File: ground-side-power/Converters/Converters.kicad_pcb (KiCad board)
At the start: 2 copper layers, 82.8 x 74.4 mm, 43 parts, among them J10 Conn_01x03_Female, J11 Ground Connections, J12 Conn_01x04_Female, J13 DAQ Voltage Sensing, J14 DAQ Current Sensing, J27 Conn_01x02_Female, U1 TPS55340, U2 K7805-3AR3, U4 INA180, U5 INA180

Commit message: implemented comments
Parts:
- added ?: , , F.Cu at (108.5, 71.1)
- added ?: , , F.Cu at (181.1, 135.6)
- added ?: , , F.Cu at (181.1, 71.1)
- added ?: , , F.Cu at (108.5, 135.6)
- added G***: LOGO, rlcs:rocketry_logo_small, F.Cu at (176.8, 125.5)
- added TP1: TestPoint, TestPoint:TestPoint_Plated_Hole_D2.0mm, F.Cu at (166.6, 111.0)
- added TP2: TestPoint, TestPoint:TestPoint_Plated_Hole_D2.0mm, F.Cu at (180.8, 88.4)
- added TP3: TestPoint, TestPoint:TestPoint_Plated_Hole_D2.0mm, F.Cu at (133.9, 76.7)
- F2: renamed from F3; value 0685T4000-01 -> 4A 0685T4000-01
- moved C10 51.8 mm to (137.7, 83.1), turned to 180 degrees
- moved C7 48.4 mm to (125.2, 81.0), turned to 180 degrees
- moved C9 41.9 mm to (144.0, 83.1), turned to 180 degrees
- moved C8 31.8 mm to (150.1, 83.1), turned to 180 degrees
- moved L1 19.8 mm to (173.7, 85.9), turned to 180 degrees
- moved C6 2.54 mm to (137.2, 99.1)
- moved R11 0.52 mm to (118.4, 129.5)
- moved D1 0.51 mm to (165.1, 85.9), turned to 0 degrees
- moved C5 0.37 mm to (152.1, 108.2), turned to -90 degrees
- renumbered C3 to C1, C12 to C10, C10 to C11, C9 to C12, C5 to C2, C7 to C3, C1 to C4, C2 to C5, C8 to C6, C4 to C7, C6 to C8, C11 to C9, D2 to D1, D5 to D2, D4 to D3, F4 to F1, J13 to J1, J14 to J2, J11 to J3, J27 to J4, J12 to J5, J10 to J6, R4 to R1, R2 to R10, R5 to R11, R6 to R12, R19 to R13, R20 to R14, R12 to R2, R18 to R3, R17 to R4, R10 to R5, R8 to R6, R3 to R7, R9 to R8, R1 to R9, U2 to U1, U1 to U2, U4 to U3, U5 to U4
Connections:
- C4 pad 1: Net-(U1-COMP) -> Net-(U2-COMP)
- C5 pad 1: GND -> Net-(U2-COMP)
- C5 pad 2: Net-(U1-COMP) -> GND
- D2 pad 1: (no net) -> Net-(D2-K)
- D2 pad 2: (no net) -> +5V
- R6 pad 1: (no net) -> Net-(D2-K)
- U2 pad 8: Net-(U1-COMP) -> Net-(U2-COMP)
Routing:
- net GND: track 404.7 -> 102.2 mm, vias 4 -> 7
- net +24V: track 110.0 -> 4.24 mm, vias 2 -> 0
- net Net-(D1-K): track 193.2 -> 87.8 mm
- net /Temp: track 101.8 -> 37.2 mm
- net +BATT: track 52.2 -> 5.56 mm
- net Net-(U1-+VO2): track 81.9 -> 53.2 mm
- net +5V: track 208.0 -> 228.1 mm
- net Net-(U2-COMP): track 0.00 -> 15.6 mm, vias 0 -> 1
- net Net-(U1-COMP): track 15.4 -> 0.00 mm, vias 1 -> 0
- net Net-(D1-A): track 14.4 -> 25.7 mm
- net Net-(D2-K): track 0.00 -> 2.64 mm
- net (no net): track 2.64 -> 0.00 mm
- net /24V_VOLTAGE: track 65.1 -> 65.9 mm
- net /5V_OUT: vias 6 -> 2
- added copper zone on F.Cu, net +24V
- added copper zone on F.Cu, net +BATT
- added copper zone on B.Cu, net GND
- removed copper zone on B.Cu, net (none)
- removed copper zone on F.Cu, net GND
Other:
- board text added: "Ground Side Power Converter Board Feb 2024 Manav Toor"

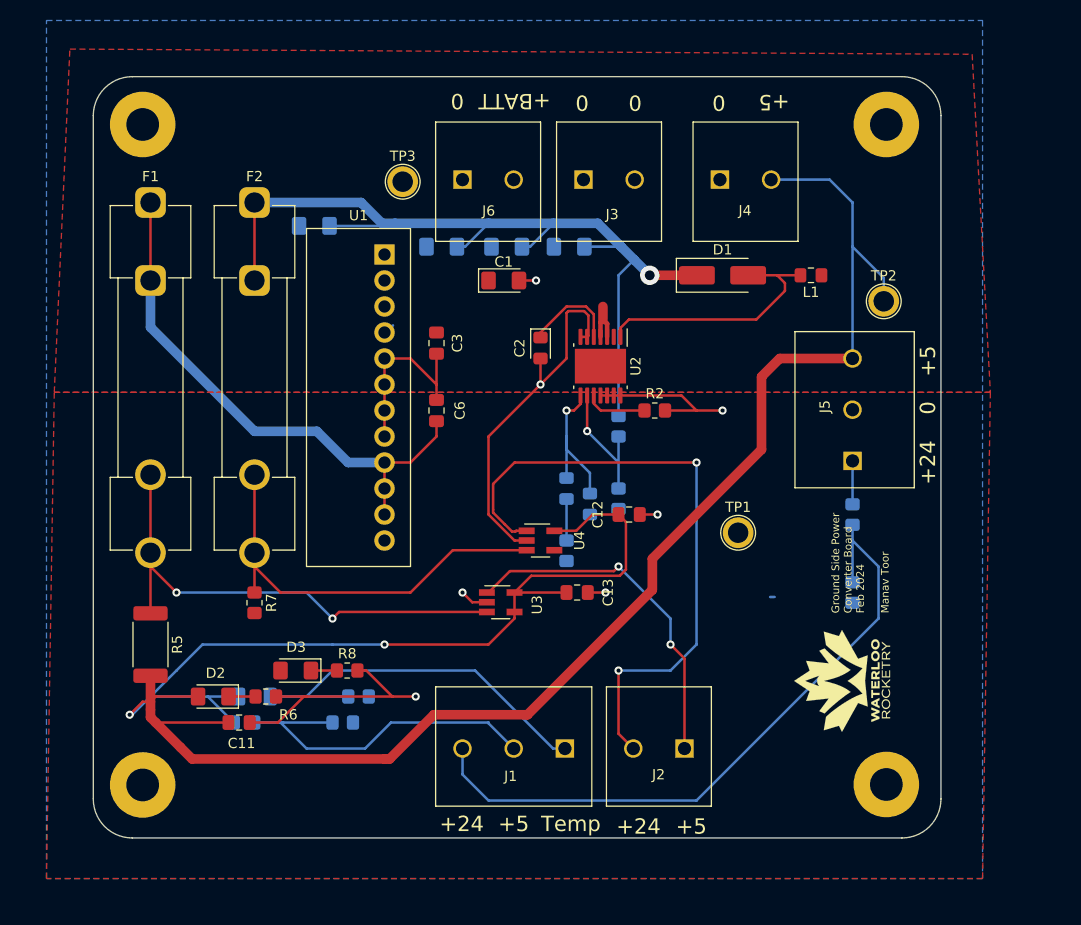
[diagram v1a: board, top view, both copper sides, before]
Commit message: sourced vertical screw terminals
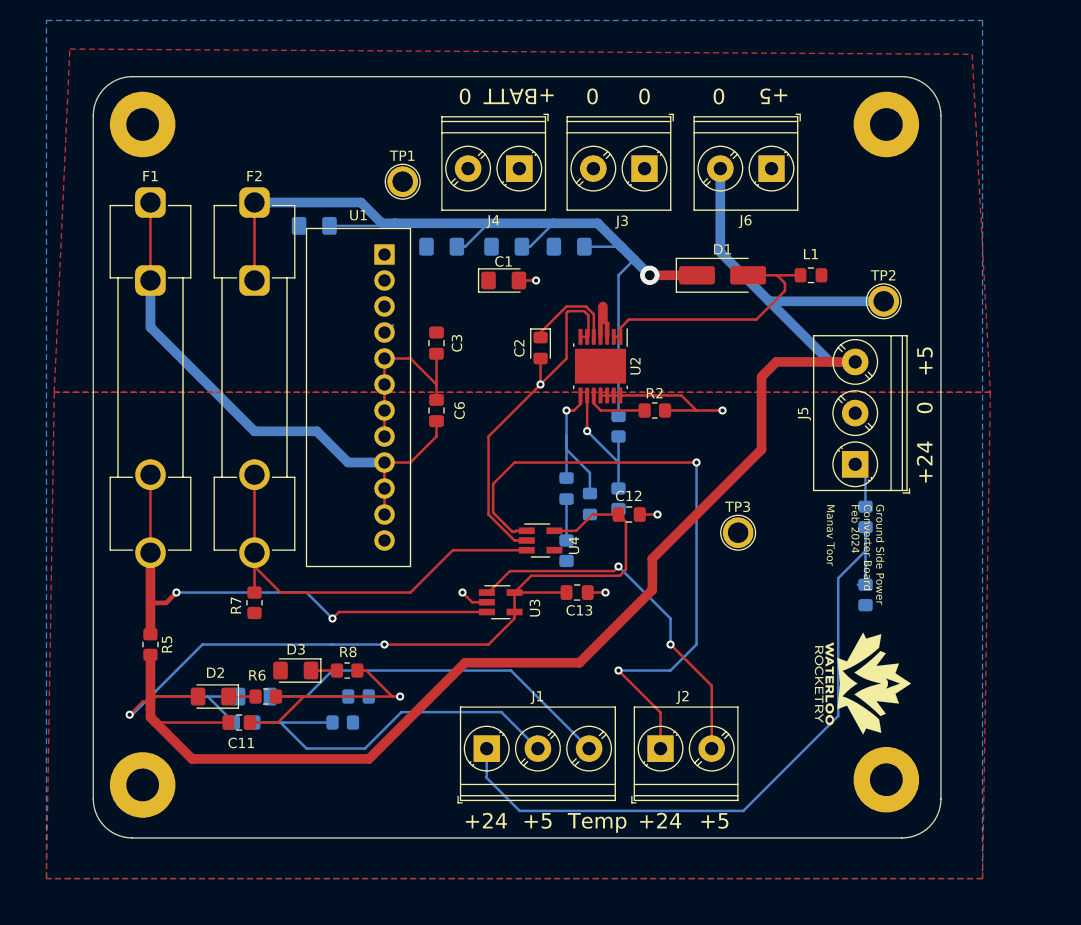
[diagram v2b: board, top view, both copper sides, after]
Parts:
- removed ? (x4): , 
- added REF**: MountingHole_3.2mm_M3_Pad, MountingHole:MountingHole_3.2mm_M3_Pad, F.Cu at (181.1, 135.1)
- added REF**: MountingHole_3.2mm_M3_Pad, MountingHole:MountingHole_3.2mm_M3_Pad, F.Cu at (181.1, 71.1)
- added REF**: MountingHole_3.2mm_M3_Pad, MountingHole:MountingHole_3.2mm_M3_Pad, F.Cu at (108.5, 135.6)
- added REF**: MountingHole_3.2mm_M3_Pad, MountingHole:MountingHole_3.2mm_M3_Pad, F.Cu at (108.5, 71.1)
- F2: value 4A 0685T4000-01 -> 3A
- J1: footprint GSP:1935323 -> TerminalBlock_Phoenix:TerminalBlock_Phoenix_PT-1,5-3-5.0-H_1x03_P5.00mm_Horizontal
- J2, J3: footprint GSP:1935310 -> TerminalBlock_Phoenix:TerminalBlock_Phoenix_PT-1,5-2-5.0-H_1x02_P5.00mm_Horizontal
- J4: value Conn_01x02_Female -> BATT_IN; footprint GSP:1935310 -> TerminalBlock_Phoenix:TerminalBlock_Phoenix_PT-1,5-2-5.0-H_1x02_P5.00mm_Horizontal
- J5: value Conn_01x04_Female -> POWER_OUT; footprint GSP:1935323 -> TerminalBlock_Phoenix:TerminalBlock_Phoenix_PT-1,5-3-5.0-H_1x03_P5.00mm_Horizontal
- J6: value Conn_01x03_Female -> 5V_IN; footprint GSP:1935310 -> TerminalBlock_Phoenix:TerminalBlock_Phoenix_PT-1,5-2-5.0-H_1x02_P5.00mm_Horizontal
- R5: footprint Resistor_SMD:R_2512_6332Metric_Pad1.40x3.35mm_HandSolder -> Resistor_SMD:R_0805_2012Metric_Pad1.20x1.40mm_HandSolder
- moved J6 30.2 mm to (169.9, 75.4), turned to 180 degrees
- moved J4 19.6 mm to (145.2, 75.4), turned to 180 degrees
- moved J1 7.63 mm to (142.1, 132.1), turned to 0 degrees
- moved J3 6.06 mm to (157.5, 75.4), turned to 180 degrees
- moved J2 2.34 mm to (159.0, 132.1), turned to 0 degrees
- moved G*** 2.05 mm to (178.8, 125.7), turned to -90 degrees
- moved R13 1.29 mm to (179.1, 109.5)
- moved R14 1.29 mm to (179.1, 117.1)
- moved J5 0.42 mm to (178.1, 104.3)
- renumbered TP3 to TP1, TP1 to TP3
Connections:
- J1 pad 1: /Temp -> /24V_VOLTAGE
- J1 pad 3: /24V_VOLTAGE -> /Temp
- J2 pad 1: /5V_OUT -> /24V_OUT
- J2 pad 2: /24V_OUT -> /5V_OUT
- J4 pad 2: +5V -> +BATT
- J6 pad 2: +BATT -> +5V
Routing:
- net +5V: track 228.1 -> 236.5 mm
- net /5V_VOLTAGE: track 33.9 -> 37.0 mm
- net /5V_Sense+: track 48.8 -> 51.5 mm
- net /Temp: track 37.2 -> 39.4 mm
- net GND: track 102.2 -> 100.2 mm
- net /24V_OUT: track 62.3 -> 63.4 mm
- net /5V_OUT: track 34.2 -> 35.3 mm
- net Net-(D1-A): track 25.7 -> 26.4 mm

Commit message: completly redid layout
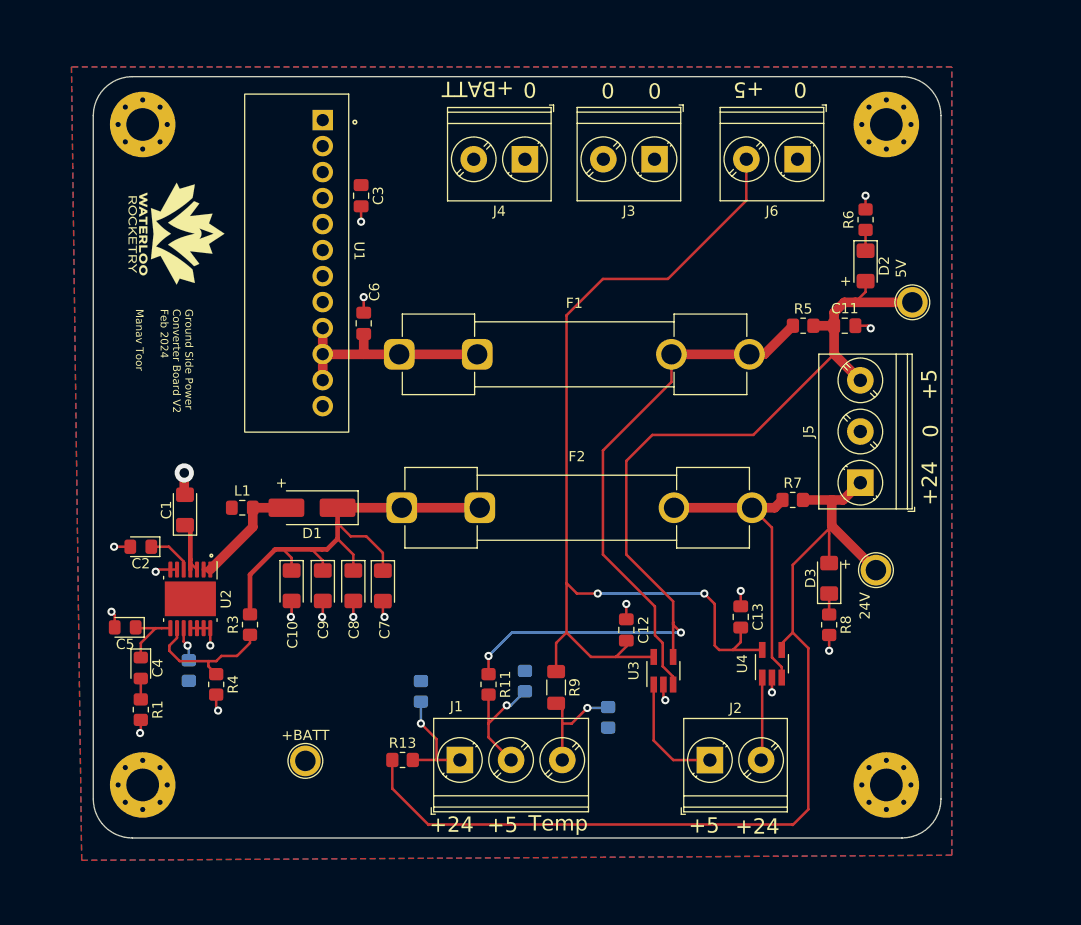
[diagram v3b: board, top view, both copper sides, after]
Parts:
- removed the REF** at (181.1, 135.1)
- removed the REF** at (181.1, 71.1)
- removed the REF** at (108.5, 135.6)
- removed the REF** at (108.5, 71.1)
- removed TP1, TP2, TP3: TestPoint, TestPoint:TestPoint_Plated_Hole_D2.0mm
- added +BATT: TestPoint, TestPoint:TestPoint_Plated_Hole_D2.0mm, F.Cu at (124.3, 133.3)
- added 24V: TestPoint, TestPoint:TestPoint_Plated_Hole_D2.0mm, F.Cu at (180.1, 114.7)
- added 5V: TestPoint, TestPoint:TestPoint_Plated_Hole_D2.0mm, F.Cu at (183.6, 88.5)
- added REF**: MountingHole_3.2mm_M3_Pad_Via, MountingHole:MountingHole_3.2mm_M3_Pad_Via, F.Cu at (108.5, 135.6)
- added REF**: MountingHole_3.2mm_M3_Pad_Via, MountingHole:MountingHole_3.2mm_M3_Pad_Via, F.Cu at (181.1, 135.6)
- added REF**: MountingHole_3.2mm_M3_Pad_Via, MountingHole:MountingHole_3.2mm_M3_Pad_Via, F.Cu at (181.1, 71.1)
- added REF**: MountingHole_3.2mm_M3_Pad_Via, MountingHole:MountingHole_3.2mm_M3_Pad_Via, F.Cu at (108.5, 71.1)
- C10, C4, C5, C7, C8, C9, R1, R11, R13, R3, R4, R9: moved to F.Cu
- R2: moved to B.Cu
- moved G*** 80.2 mm to (111.8, 81.8)
- moved D2 76.3 mm to (179.1, 84.9), turned to -90 degrees
- moved R6 74.8 mm to (179.1, 80.4), turned to 90 degrees
- moved R5 71.0 mm to (173.0, 90.8), turned to 0 degrees
- moved C11 70.7 mm to (177.0, 90.8)
- moved L1 60.0 mm to (118.2, 108.6), turned to 0 degrees
- moved R7 53.5 mm to (172.0, 107.8), turned to 0 degrees
- moved D3 52.9 mm to (175.5, 115.5), turned to 90 degrees
- moved R2 52.1 mm to (113.0, 124.5), turned to -90 degrees
- moved R13 51.1 mm to (133.8, 133.2), turned to 0 degrees
- moved R8 47.3 mm to (175.5, 120.0), turned to -90 degrees
- moved C5 47.0 mm to (106.7, 120.2), turned to 180 degrees
- moved D1 46.1 mm to (125.0, 108.6), turned to 180 degrees
- moved U2 46.1 mm to (113.1, 117.5)
- moved C4 45.1 mm to (108.3, 124.2)
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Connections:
- J2 pad 1: /24V_OUT -> /5V_OUT
- J2 pad 2: /5V_OUT -> /24V_OUT
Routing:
- net +24V: track 4.15 -> 96.3 mm
- net GND: track 100.2 -> 34.2 mm, vias 7 -> 20
- net /24V_OUT: track 63.4 -> 8.10 mm, vias 2 -> 0
- net /24V_VOLTAGE: track 65.9 -> 10.9 mm, vias 0 -> 1
- net +5V: track 236.5 -> 188.4 mm, vias 2 -> 4
- net Net-(D1-K): track 87.8 -> 47.8 mm, vias 1 -> 0
- net Net-(U1-+VO2): track 53.2 -> 22.2 mm
- net /Temp: track 39.4 -> 10.9 mm, vias 0 -> 1
- net /5V_VOLTAGE: track 37.0 -> 12.2 mm, vias 0 -> 1
- net /5V_OUT: track 35.3 -> 11.8 mm, vias 2 -> 0
- net Net-(D1-A): track 26.4 -> 11.7 mm
- net /24V_Sense+: track 40.9 -> 28.7 mm
- net Net-(U2-COMP): track 15.6 -> 6.89 mm, vias 1 -> 0
- net Net-(U2-SS): track 9.27 -> 4.55 mm
- net Net-(U2-FREQ): track 6.02 -> 3.34 mm, vias 0 -> 1
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- removed copper zone on F.Cu, net +24V
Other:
- board text added: "+"
- board text added: "Ground Side Power Converter Board V2 Feb 2024 Manav Toor"
- board text removed: "Ground Side Power Converter Board Feb 2024 Manav Toor"

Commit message: added inductor footprint
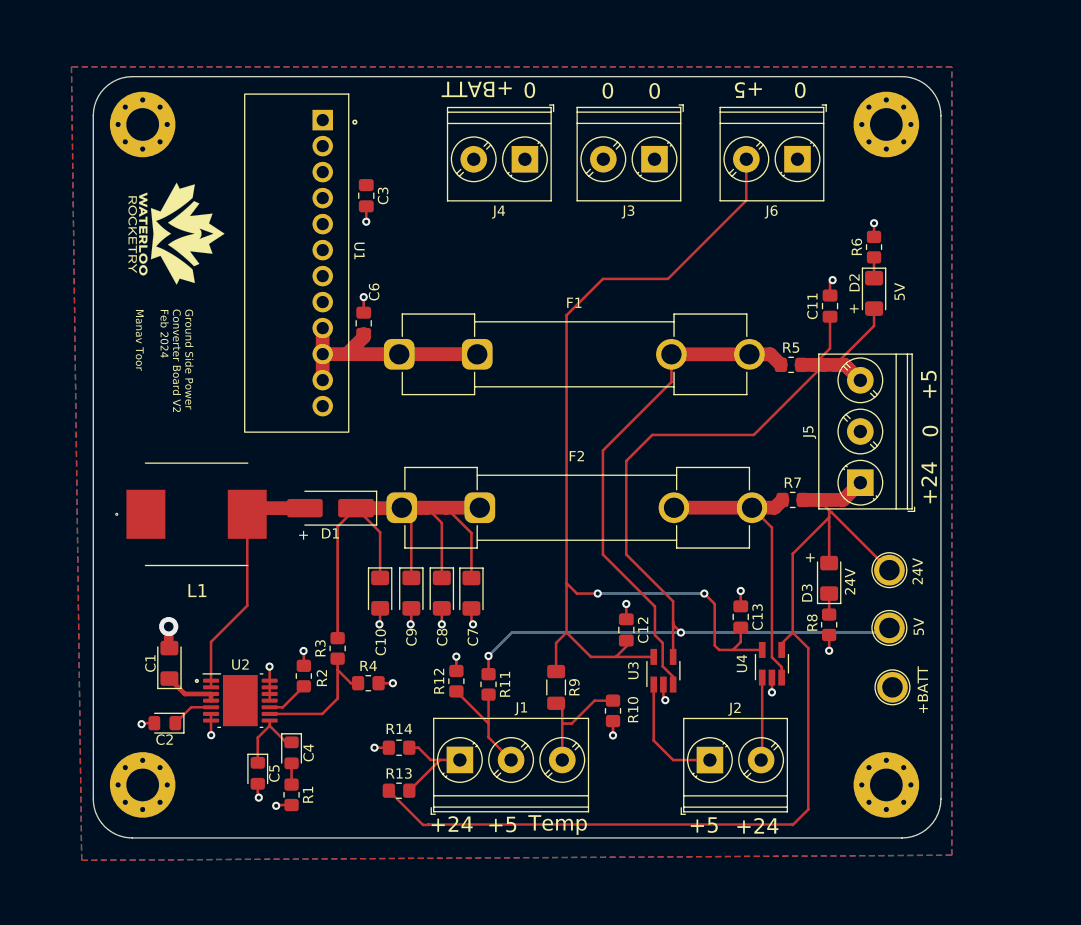
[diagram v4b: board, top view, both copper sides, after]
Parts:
- L1: footprint Inductor_SMD:L_0805_2012Metric_Pad1.15x1.40mm_HandSolder -> ETQ-P5M100YFC:ETQP5M_YFC_YGC
- R10, R12, R14, R2: moved to F.Cu
- moved +BATT 57.8 mm to (181.7, 126.1), turned to 90 degrees
- moved 5V 31.9 mm to (181.4, 120.3)
- moved C5 19.3 mm to (119.7, 134.5), turned to -90 degrees
- moved C2 17.4 mm to (110.6, 129.6)
- moved R1 16.9 mm to (123.0, 136.6)
- moved C4 16.9 mm to (123.0, 132.5)
- moved C1 15.1 mm to (111.1, 123.8)
- moved R4 14.9 mm to (130.5, 125.7), turned to 0 degrees
- moved R2 11.3 mm to (124.2, 125.0), turned to 90 degrees
- moved U2 11.1 mm to (118.0, 127.4), turned to 0 degrees
- moved R3 8.87 mm to (127.5, 122.3)
- moved C7 8.68 mm to (140.6, 116.9)
- moved C10 8.68 mm to (131.7, 116.9)
- moved C8 8.68 mm to (137.7, 116.9)
- moved C9 8.68 mm to (134.7, 116.9)
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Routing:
- net +5V: track 188.4 -> 206.1 mm
- net Net-(D1-A): track 11.7 -> 24.5 mm
- net Net-(D1-K): track 47.8 -> 57.2 mm
- net GND: track 34.2 -> 38.7 mm, vias 20 -> 24
- net /5V_Sense+: track 50.9 -> 49.0 mm
- net /24V_VOLTAGE: track 10.9 -> 9.69 mm, vias 1 -> 0
- net +24V: track 96.3 -> 97.2 mm
- net Net-(U2-FREQ): track 3.34 -> 4.19 mm, vias 1 -> 0
- net /Temp: track 10.9 -> 11.7 mm, vias 1 -> 0
- net Net-(U1-+VO2): track 22.2 -> 22.9 mm
- net Net-(U2-COMP): track 6.89 -> 7.41 mm
- net /5V_VOLTAGE: track 12.2 -> 11.7 mm, vias 1 -> 0
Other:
- board text added: "24V"
- board text added: "5V"
